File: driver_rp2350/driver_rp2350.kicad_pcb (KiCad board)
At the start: 6 copper layers, 45 x 45 mm, 0 parts

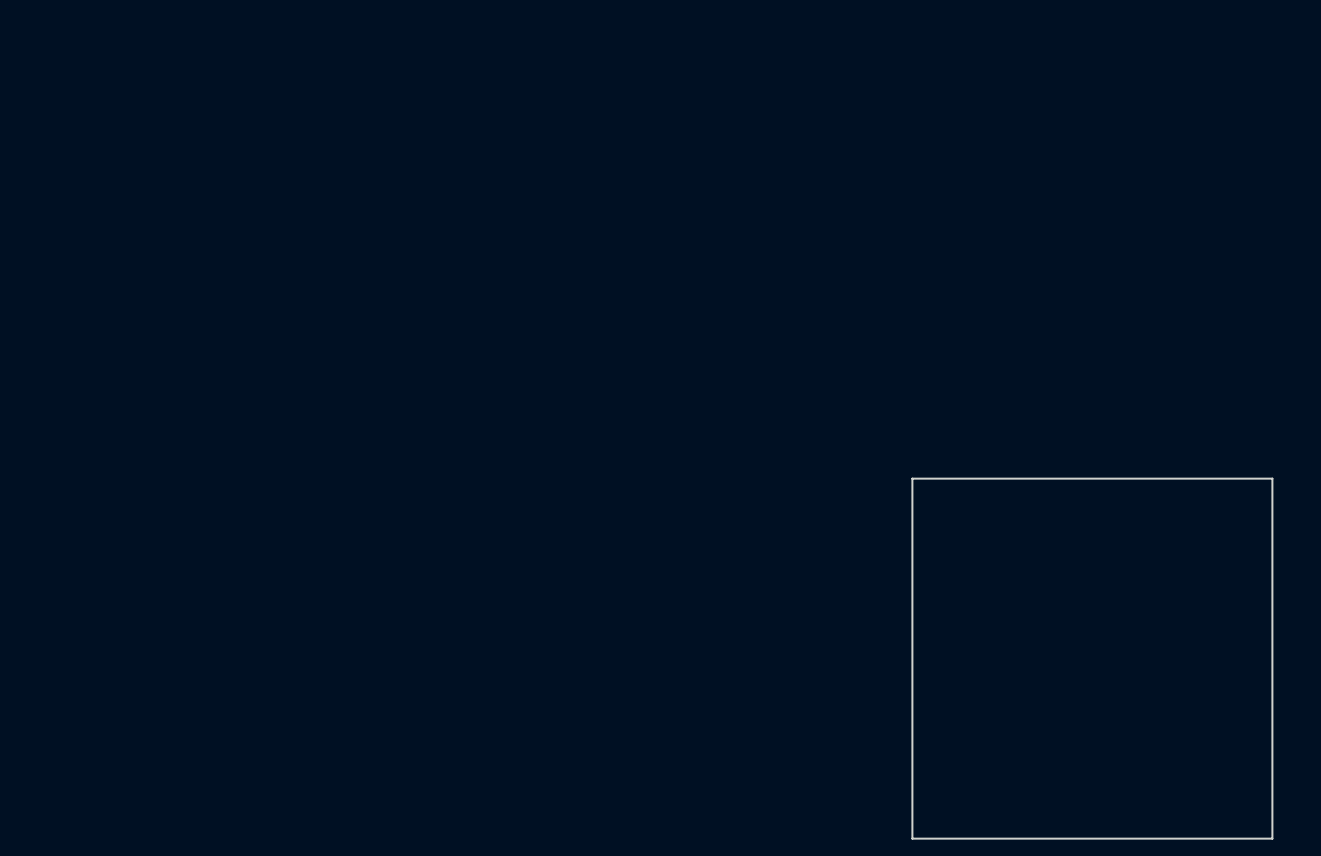
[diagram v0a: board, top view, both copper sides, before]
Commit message: Worked on rp2350 driver layout.
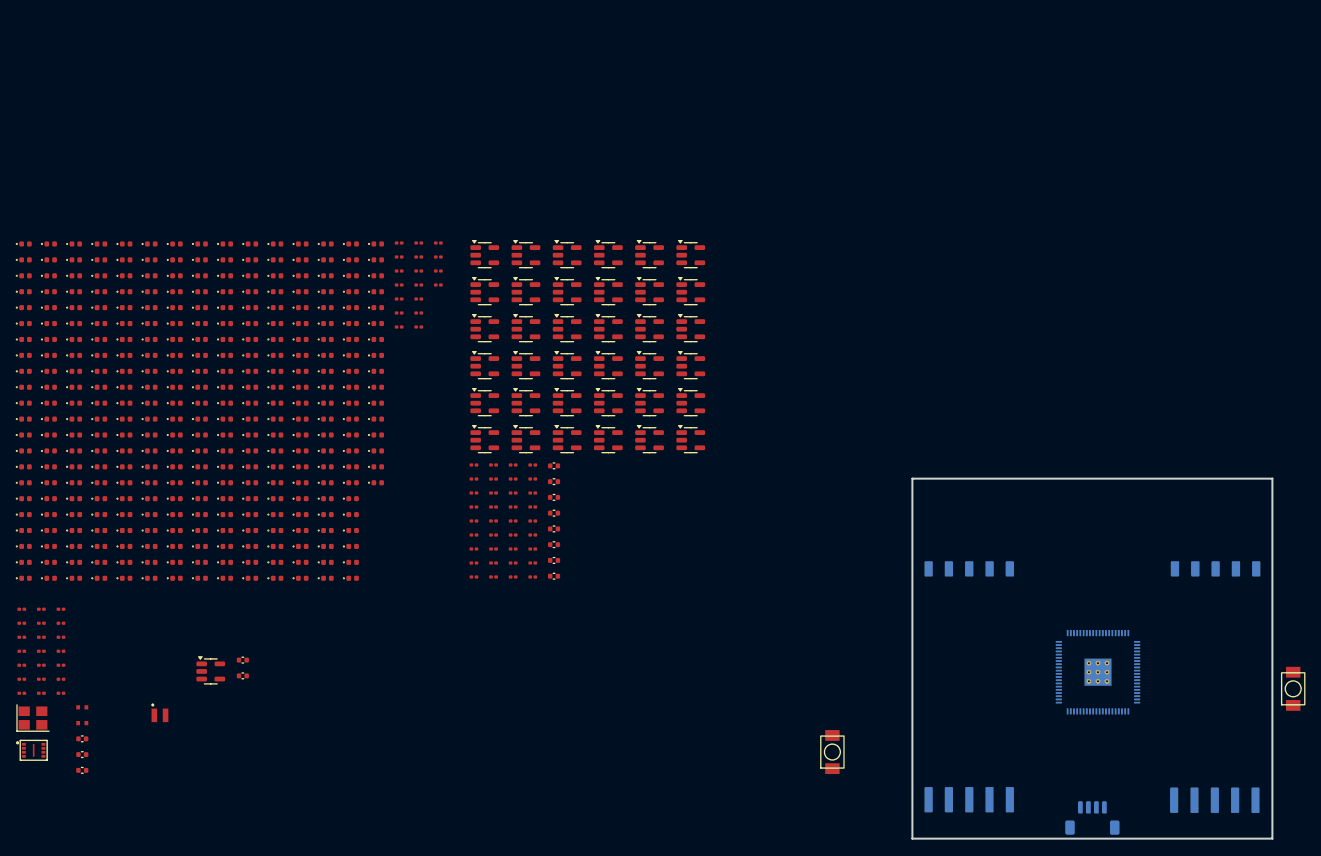
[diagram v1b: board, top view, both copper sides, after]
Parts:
- added C1: 15pF, Capacitor_SMD:C_0201_0603Metric, F.Cu at (-61.3, 66.3)
- added C10: 100nF, Capacitor_SMD:C_0201_0603Metric, F.Cu at (-61.3, 75.1)
- added C11: 100nF, Capacitor_SMD:C_0201_0603Metric, F.Cu at (-61.3, 76.8)
- added C12: 100nF, Capacitor_SMD:C_0201_0603Metric, F.Cu at (-58.9, 66.3)
- added C13: 100nF, Capacitor_SMD:C_0201_0603Metric, F.Cu at (-58.9, 68.1)
- added C14: 100nF, Capacitor_SMD:C_0201_0603Metric, F.Cu at (-58.9, 69.8)
- added C15: 100nF, Capacitor_SMD:C_0201_0603Metric, F.Cu at (-58.9, 71.6)
- added C16: 100nF, Capacitor_SMD:C_0201_0603Metric, F.Cu at (-58.9, 73.3)
- added C17: 100nF, Capacitor_SMD:C_0201_0603Metric, F.Cu at (-58.9, 75.1)
- added C18: 100nF, Capacitor_SMD:C_0201_0603Metric, F.Cu at (-58.9, 76.8)
- added C19: 10uF, Capacitor_SMD:C_0402_1005Metric, F.Cu at (-53.8, 86.5)
- added C2: 15pF, Capacitor_SMD:C_0201_0603Metric, F.Cu at (-61.3, 68.1)
- added C20: 100nF, Capacitor_SMD:C_0201_0603Metric, F.Cu at (-4.80, 48.3)
- added C21: 100nF, Capacitor_SMD:C_0201_0603Metric, F.Cu at (-4.80, 50.0)
- added C22: 100nF, Capacitor_SMD:C_0201_0603Metric, F.Cu at (-4.80, 51.8)
- added C23: 100nF, Capacitor_SMD:C_0201_0603Metric, F.Cu at (-4.80, 53.5)
- added C24: 100nF, Capacitor_SMD:C_0201_0603Metric, F.Cu at (-4.80, 55.3)
- added C25: 100nF, Capacitor_SMD:C_0201_0603Metric, F.Cu at (-4.80, 57.0)
- added C26: 100nF, Capacitor_SMD:C_0201_0603Metric, F.Cu at (-4.80, 58.8)
- added C27: 100nF, Capacitor_SMD:C_0201_0603Metric, F.Cu at (-4.80, 60.5)
- added C28: 100nF, Capacitor_SMD:C_0201_0603Metric, F.Cu at (-4.80, 62.3)
- added C29: 100nF, Capacitor_SMD:C_0201_0603Metric, F.Cu at (-2.35, 48.3)
- added C3: 100nF, Capacitor_SMD:C_0201_0603Metric, F.Cu at (-61.3, 69.8)
- added C30: 100nF, Capacitor_SMD:C_0201_0603Metric, F.Cu at (-2.35, 50.0)
- added C31: 100nF, Capacitor_SMD:C_0201_0603Metric, F.Cu at (-2.35, 51.8)
- added C32: 100nF, Capacitor_SMD:C_0201_0603Metric, F.Cu at (-2.35, 53.5)
- added C33: 100nF, Capacitor_SMD:C_0201_0603Metric, F.Cu at (-2.35, 55.3)
- added C34: 100nF, Capacitor_SMD:C_0201_0603Metric, F.Cu at (-2.35, 57.0)
- added C35: 100nF, Capacitor_SMD:C_0201_0603Metric, F.Cu at (-2.35, 58.8)
- added C36: 100nF, Capacitor_SMD:C_0201_0603Metric, F.Cu at (-2.35, 60.5)
- added C37: 100nF, Capacitor_SMD:C_0201_0603Metric, F.Cu at (-2.35, 62.3)
- added C38: 100nF, Capacitor_SMD:C_0201_0603Metric, F.Cu at (0.10, 48.3)
- added C39: 100nF, Capacitor_SMD:C_0201_0603Metric, F.Cu at (0.10, 50.0)
- added C4: 4.7uF, RP2350_80QFN_minimal:C_0402_1005Metric_small_pads, F.Cu at (-53.8, 78.6)
- added C40: 100nF, Capacitor_SMD:C_0201_0603Metric, F.Cu at (0.10, 51.8)
- added C41: 100nF, Capacitor_SMD:C_0201_0603Metric, F.Cu at (0.10, 53.5)
- added C42: 100nF, Capacitor_SMD:C_0201_0603Metric, F.Cu at (0.10, 55.3)
- added C43: 100nF, Capacitor_SMD:C_0201_0603Metric, F.Cu at (0.10, 57.0)
- added C44: 100nF, Capacitor_SMD:C_0201_0603Metric, F.Cu at (0.10, 58.8)
- added C45: 100nF, Capacitor_SMD:C_0201_0603Metric, F.Cu at (0.10, 60.5)
- added C46: 100nF, Capacitor_SMD:C_0201_0603Metric, F.Cu at (0.10, 62.3)
- added C47: 100nF, Capacitor_SMD:C_0201_0603Metric, F.Cu at (2.54, 48.3)
- added C48: 100nF, Capacitor_SMD:C_0201_0603Metric, F.Cu at (2.54, 50.0)
- added C49: 100nF, Capacitor_SMD:C_0201_0603Metric, F.Cu at (2.54, 51.8)
- added C5: 4.7uF, RP2350_80QFN_minimal:C_0402_1005Metric_small_pads, F.Cu at (-53.8, 80.6)
- added C50: 100nF, Capacitor_SMD:C_0201_0603Metric, F.Cu at (2.54, 53.5)
- added C51: 100nF, Capacitor_SMD:C_0201_0603Metric, F.Cu at (2.54, 55.3)
- added C52: 100nF, Capacitor_SMD:C_0201_0603Metric, F.Cu at (2.54, 57.0)
- added C53: 100nF, Capacitor_SMD:C_0201_0603Metric, F.Cu at (2.54, 58.8)
- added C54: 100nF, Capacitor_SMD:C_0201_0603Metric, F.Cu at (2.54, 60.5)
- added C55: 100nF, Capacitor_SMD:C_0201_0603Metric, F.Cu at (2.54, 62.3)
- added C56: 10uF, Capacitor_SMD:C_0402_1005Metric, F.Cu at (5.21, 48.4)
- added C57: 10uF, Capacitor_SMD:C_0402_1005Metric, F.Cu at (5.21, 50.4)
- added C58: 10uF, Capacitor_SMD:C_0402_1005Metric, F.Cu at (5.21, 52.3)
- added C59: 10uF, Capacitor_SMD:C_0402_1005Metric, F.Cu at (5.21, 54.3)
- added C6: 100nF, Capacitor_SMD:C_0201_0603Metric, F.Cu at (-61.3, 71.6)
- added C60: 10uF, Capacitor_SMD:C_0402_1005Metric, F.Cu at (5.21, 56.3)
- added C61: 10uF, Capacitor_SMD:C_0402_1005Metric, F.Cu at (5.21, 58.3)
- added C62: 10uF, Capacitor_SMD:C_0402_1005Metric, F.Cu at (5.21, 60.2)
- added C63: 10uF, Capacitor_SMD:C_0402_1005Metric, F.Cu at (5.21, 62.2)
- added C64: 10uF, Capacitor_SMD:C_0402_1005Metric, F.Cu at (-33.7, 72.7)
- added C65: 10uF, Capacitor_SMD:C_0402_1005Metric, F.Cu at (-33.7, 74.7)
- added C7: 4.7uF, Capacitor_SMD:C_0402_1005Metric, F.Cu at (-53.8, 82.5)
- added C8: 4.7uF, Capacitor_SMD:C_0402_1005Metric, F.Cu at (-53.8, 84.5)
- added C9: 100nF, Capacitor_SMD:C_0201_0603Metric, F.Cu at (-61.3, 73.3)
- added D_0A1: LED, panel_custom:LED_0402_1005Metric, F.Cu at (-48.3, 44.5)
- added D_0B1: LED, panel_custom:LED_0402_1005Metric, F.Cu at (-48.3, 46.5)
- added D_0C1: LED, panel_custom:LED_0402_1005Metric, F.Cu at (-48.3, 48.5)
- added D_0D1: LED, panel_custom:LED_0402_1005Metric, F.Cu at (-48.3, 50.5)
- added D_0E1: LED, panel_custom:LED_0402_1005Metric, F.Cu at (-48.3, 52.5)
- added D_0F1: LED, panel_custom:LED_0402_1005Metric, F.Cu at (-48.3, 54.5)
- added D_0G1: LED, panel_custom:LED_0402_1005Metric, F.Cu at (-48.3, 56.5)
- added D_0H1: LED, panel_custom:LED_0402_1005Metric, F.Cu at (-48.3, 58.5)
- added D_1: LED, panel_custom:LED_0402_1005Metric, F.Cu at (-60.9, 20.7)
- added D_10: LED, panel_custom:LED_0402_1005Metric, F.Cu at (-60.9, 38.6)
- added D_100: LED, panel_custom:LED_0402_1005Metric, F.Cu at (-48.3, 42.6)
- added D_11: LED, panel_custom:LED_0402_1005Metric, F.Cu at (-60.9, 40.6)
- added D_12: LED, panel_custom:LED_0402_1005Metric, F.Cu at (-60.9, 42.6)
- added D_13: LED, panel_custom:LED_0402_1005Metric, F.Cu at (-60.9, 44.5)
- added D_14: LED, panel_custom:LED_0402_1005Metric, F.Cu at (-60.9, 46.5)
- added D_15: LED, panel_custom:LED_0402_1005Metric, F.Cu at (-60.9, 48.5)
- added D_16: LED, panel_custom:LED_0402_1005Metric, F.Cu at (-60.9, 50.5)
- added D_17: LED, panel_custom:LED_0402_1005Metric, F.Cu at (-60.9, 52.5)
- added D_18: LED, panel_custom:LED_0402_1005Metric, F.Cu at (-60.9, 54.5)
- added D_19: LED, panel_custom:LED_0402_1005Metric, F.Cu at (-60.9, 56.5)
- added D_1A1: LED, panel_custom:LED_0402_1005Metric, F.Cu at (-48.3, 60.5)
- added D_1B1: LED, panel_custom:LED_0402_1005Metric, F.Cu at (-48.3, 62.5)
- added D_1C1: LED, panel_custom:LED_0402_1005Metric, F.Cu at (-45.1, 20.7)
- added D_1D1: LED, panel_custom:LED_0402_1005Metric, F.Cu at (-45.1, 22.7)
- added D_1E1: LED, panel_custom:LED_0402_1005Metric, F.Cu at (-45.1, 24.6)
- added D_1F1: LED, panel_custom:LED_0402_1005Metric, F.Cu at (-45.1, 26.6)
- added D_1G1: LED, panel_custom:LED_0402_1005Metric, F.Cu at (-45.1, 28.6)
- added D_1H1: LED, panel_custom:LED_0402_1005Metric, F.Cu at (-45.1, 30.6)
- added D_2: LED, panel_custom:LED_0402_1005Metric, F.Cu at (-60.9, 22.7)
- added D_20: LED, panel_custom:LED_0402_1005Metric, F.Cu at (-60.9, 58.5)
- added D_21: LED, panel_custom:LED_0402_1005Metric, F.Cu at (-60.9, 60.5)
- added D_22: LED, panel_custom:LED_0402_1005Metric, F.Cu at (-60.9, 62.5)
- added D_23: LED, panel_custom:LED_0402_1005Metric, F.Cu at (-57.7, 20.7)
- added D_24: LED, panel_custom:LED_0402_1005Metric, F.Cu at (-57.7, 22.7)
- added D_25: LED, panel_custom:LED_0402_1005Metric, F.Cu at (-57.7, 24.6)
- added D_26: LED, panel_custom:LED_0402_1005Metric, F.Cu at (-57.7, 26.6)
- added D_27: LED, panel_custom:LED_0402_1005Metric, F.Cu at (-57.7, 28.6)
- added D_28: LED, panel_custom:LED_0402_1005Metric, F.Cu at (-57.7, 30.6)
- added D_29: LED, panel_custom:LED_0402_1005Metric, F.Cu at (-57.7, 32.6)
- added D_2A1: LED, panel_custom:LED_0402_1005Metric, F.Cu at (-45.1, 32.6)
- added D_2B1: LED, panel_custom:LED_0402_1005Metric, F.Cu at (-45.1, 34.6)
- added D_2C1: LED, panel_custom:LED_0402_1005Metric, F.Cu at (-45.1, 36.6)
- added D_2D1: LED, panel_custom:LED_0402_1005Metric, F.Cu at (-45.1, 38.6)
- added D_2E1: LED, panel_custom:LED_0402_1005Metric, F.Cu at (-45.1, 40.6)
- added D_2F1: LED, panel_custom:LED_0402_1005Metric, F.Cu at (-45.1, 42.6)
- added D_2G1: LED, panel_custom:LED_0402_1005Metric, F.Cu at (-45.1, 44.5)
- added D_2H1: LED, panel_custom:LED_0402_1005Metric, F.Cu at (-45.1, 46.5)
- added D_3: LED, panel_custom:LED_0402_1005Metric, F.Cu at (-60.9, 24.6)
- added D_30: LED, panel_custom:LED_0402_1005Metric, F.Cu at (-57.7, 34.6)
- added D_31: LED, panel_custom:LED_0402_1005Metric, F.Cu at (-57.7, 36.6)
- added D_32: LED, panel_custom:LED_0402_1005Metric, F.Cu at (-57.7, 38.6)
- added D_33: LED, panel_custom:LED_0402_1005Metric, F.Cu at (-57.7, 40.6)
- added D_34: LED, panel_custom:LED_0402_1005Metric, F.Cu at (-57.7, 42.6)
- added D_35: LED, panel_custom:LED_0402_1005Metric, F.Cu at (-57.7, 44.5)
- added D_36: LED, panel_custom:LED_0402_1005Metric, F.Cu at (-57.7, 46.5)
- added D_37: LED, panel_custom:LED_0402_1005Metric, F.Cu at (-57.7, 48.5)
- added D_38: LED, panel_custom:LED_0402_1005Metric, F.Cu at (-57.7, 50.5)
- added D_39: LED, panel_custom:LED_0402_1005Metric, F.Cu at (-57.7, 52.5)
- added D_3A1: LED, panel_custom:LED_0402_1005Metric, F.Cu at (-45.1, 48.5)
- added D_3B1: LED, panel_custom:LED_0402_1005Metric, F.Cu at (-45.1, 50.5)
- added D_3C1: LED, panel_custom:LED_0402_1005Metric, F.Cu at (-45.1, 52.5)
- added D_3D1: LED, panel_custom:LED_0402_1005Metric, F.Cu at (-45.1, 54.5)
- added D_3E1: LED, panel_custom:LED_0402_1005Metric, F.Cu at (-45.1, 56.5)
- added D_3F1: LED, panel_custom:LED_0402_1005Metric, F.Cu at (-45.1, 58.5)
- added D_3G1: LED, panel_custom:LED_0402_1005Metric, F.Cu at (-45.1, 60.5)
- added D_3H1: LED, panel_custom:LED_0402_1005Metric, F.Cu at (-45.1, 62.5)
- added D_4: LED, panel_custom:LED_0402_1005Metric, F.Cu at (-60.9, 26.6)
- added D_40: LED, panel_custom:LED_0402_1005Metric, F.Cu at (-57.7, 54.5)
- added D_41: LED, panel_custom:LED_0402_1005Metric, F.Cu at (-57.7, 56.5)
- added D_42: LED, panel_custom:LED_0402_1005Metric, F.Cu at (-57.7, 58.5)
- added D_43: LED, panel_custom:LED_0402_1005Metric, F.Cu at (-57.7, 60.5)
- added D_44: LED, panel_custom:LED_0402_1005Metric, F.Cu at (-57.7, 62.5)
- added D_45: LED, panel_custom:LED_0402_1005Metric, F.Cu at (-54.6, 20.7)
- added D_46: LED, panel_custom:LED_0402_1005Metric, F.Cu at (-54.6, 22.7)
- added D_47: LED, panel_custom:LED_0402_1005Metric, F.Cu at (-54.6, 24.6)
- added D_48: LED, panel_custom:LED_0402_1005Metric, F.Cu at (-54.6, 26.6)
- added D_49: LED, panel_custom:LED_0402_1005Metric, F.Cu at (-54.6, 28.6)
- added D_4A1: LED, panel_custom:LED_0402_1005Metric, F.Cu at (-42.0, 20.7)
- added D_4B1: LED, panel_custom:LED_0402_1005Metric, F.Cu at (-42.0, 22.7)
- added D_4C1: LED, panel_custom:LED_0402_1005Metric, F.Cu at (-42.0, 24.6)
- added D_4D1: LED, panel_custom:LED_0402_1005Metric, F.Cu at (-42.0, 26.6)
- added D_4E1: LED, panel_custom:LED_0402_1005Metric, F.Cu at (-42.0, 28.6)
- added D_4F1: LED, panel_custom:LED_0402_1005Metric, F.Cu at (-42.0, 30.6)
- added D_4G1: LED, panel_custom:LED_0402_1005Metric, F.Cu at (-42.0, 32.6)
- added D_4H1: LED, panel_custom:LED_0402_1005Metric, F.Cu at (-42.0, 34.6)
- added D_5: LED, panel_custom:LED_0402_1005Metric, F.Cu at (-60.9, 28.6)
- added D_50: LED, panel_custom:LED_0402_1005Metric, F.Cu at (-54.6, 30.6)
- added D_51: LED, panel_custom:LED_0402_1005Metric, F.Cu at (-54.6, 32.6)
- added D_52: LED, panel_custom:LED_0402_1005Metric, F.Cu at (-54.6, 34.6)
- added D_53: LED, panel_custom:LED_0402_1005Metric, F.Cu at (-54.6, 36.6)
- added D_54: LED, panel_custom:LED_0402_1005Metric, F.Cu at (-54.6, 38.6)
- added D_55: LED, panel_custom:LED_0402_1005Metric, F.Cu at (-54.6, 40.6)
- added D_56: LED, panel_custom:LED_0402_1005Metric, F.Cu at (-54.6, 42.6)
- added D_57: LED, panel_custom:LED_0402_1005Metric, F.Cu at (-54.6, 44.5)
- added D_58: LED, panel_custom:LED_0402_1005Metric, F.Cu at (-54.6, 46.5)
- added D_59: LED, panel_custom:LED_0402_1005Metric, F.Cu at (-54.6, 48.5)
- added D_5A1: LED, panel_custom:LED_0402_1005Metric, F.Cu at (-42.0, 36.6)
- added D_5B1: LED, panel_custom:LED_0402_1005Metric, F.Cu at (-42.0, 38.6)
- added D_5C1: LED, panel_custom:LED_0402_1005Metric, F.Cu at (-42.0, 40.6)
- added D_5D1: LED, panel_custom:LED_0402_1005Metric, F.Cu at (-42.0, 42.6)
- added D_5E1: LED, panel_custom:LED_0402_1005Metric, F.Cu at (-42.0, 44.5)
- added D_5F1: LED, panel_custom:LED_0402_1005Metric, F.Cu at (-42.0, 46.5)
- added D_5G1: LED, panel_custom:LED_0402_1005Metric, F.Cu at (-42.0, 48.5)
- added D_5H1: LED, panel_custom:LED_0402_1005Metric, F.Cu at (-42.0, 50.5)
- added D_6: LED, panel_custom:LED_0402_1005Metric, F.Cu at (-60.9, 30.6)
- added D_60: LED, panel_custom:LED_0402_1005Metric, F.Cu at (-54.6, 50.5)
- added D_61: LED, panel_custom:LED_0402_1005Metric, F.Cu at (-54.6, 52.5)
- added D_62: LED, panel_custom:LED_0402_1005Metric, F.Cu at (-54.6, 54.5)
- added D_63: LED, panel_custom:LED_0402_1005Metric, F.Cu at (-54.6, 56.5)
- added D_64: LED, panel_custom:LED_0402_1005Metric, F.Cu at (-54.6, 58.5)
- added D_65: LED, panel_custom:LED_0402_1005Metric, F.Cu at (-54.6, 60.5)
- added D_66: LED, panel_custom:LED_0402_1005Metric, F.Cu at (-54.6, 62.5)
- added D_67: LED, panel_custom:LED_0402_1005Metric, F.Cu at (-51.4, 20.7)
- added D_68: LED, panel_custom:LED_0402_1005Metric, F.Cu at (-51.4, 22.7)
- added D_69: LED, panel_custom:LED_0402_1005Metric, F.Cu at (-51.4, 24.6)
- added D_6A1: LED, panel_custom:LED_0402_1005Metric, F.Cu at (-42.0, 52.5)
- added D_6B1: LED, panel_custom:LED_0402_1005Metric, F.Cu at (-42.0, 54.5)
- added D_6C1: LED, panel_custom:LED_0402_1005Metric, F.Cu at (-42.0, 56.5)
- added D_6D1: LED, panel_custom:LED_0402_1005Metric, F.Cu at (-42.0, 58.5)
- added D_6E1: LED, panel_custom:LED_0402_1005Metric, F.Cu at (-42.0, 60.5)
- added D_6F1: LED, panel_custom:LED_0402_1005Metric, F.Cu at (-42.0, 62.5)
- added D_6G1: LED, panel_custom:LED_0402_1005Metric, F.Cu at (-38.8, 20.7)
- added D_6H1: LED, panel_custom:LED_0402_1005Metric, F.Cu at (-38.8, 22.7)
- added D_7: LED, panel_custom:LED_0402_1005Metric, F.Cu at (-60.9, 32.6)
- added D_70: LED, panel_custom:LED_0402_1005Metric, F.Cu at (-51.4, 26.6)
- added D_71: LED, panel_custom:LED_0402_1005Metric, F.Cu at (-51.4, 28.6)
- added D_72: LED, panel_custom:LED_0402_1005Metric, F.Cu at (-51.4, 30.6)
- added D_73: LED, panel_custom:LED_0402_1005Metric, F.Cu at (-51.4, 32.6)
- added D_74: LED, panel_custom:LED_0402_1005Metric, F.Cu at (-51.4, 34.6)
- added D_75: LED, panel_custom:LED_0402_1005Metric, F.Cu at (-51.4, 36.6)
- added D_76: LED, panel_custom:LED_0402_1005Metric, F.Cu at (-51.4, 38.6)
- added D_77: LED, panel_custom:LED_0402_1005Metric, F.Cu at (-51.4, 40.6)
- added D_78: LED, panel_custom:LED_0402_1005Metric, F.Cu at (-51.4, 42.6)
- added D_79: LED, panel_custom:LED_0402_1005Metric, F.Cu at (-51.4, 44.5)
- added D_7A1: LED, panel_custom:LED_0402_1005Metric, F.Cu at (-38.8, 24.6)
- added D_7B1: LED, panel_custom:LED_0402_1005Metric, F.Cu at (-38.8, 26.6)
- added D_7C1: LED, panel_custom:LED_0402_1005Metric, F.Cu at (-38.8, 28.6)
- added D_7D1: LED, panel_custom:LED_0402_1005Metric, F.Cu at (-38.8, 30.6)
- added D_7E1: LED, panel_custom:LED_0402_1005Metric, F.Cu at (-38.8, 32.6)
- added D_7F1: LED, panel_custom:LED_0402_1005Metric, F.Cu at (-38.8, 34.6)
- added D_7G1: LED, panel_custom:LED_0402_1005Metric, F.Cu at (-38.8, 36.6)
- added D_7H1: LED, panel_custom:LED_0402_1005Metric, F.Cu at (-38.8, 38.6)
- added D_8: LED, panel_custom:LED_0402_1005Metric, F.Cu at (-60.9, 34.6)
- added D_80: LED, panel_custom:LED_0402_1005Metric, F.Cu at (-51.4, 46.5)
- added D_81: LED, panel_custom:LED_0402_1005Metric, F.Cu at (-51.4, 48.5)
- added D_82: LED, panel_custom:LED_0402_1005Metric, F.Cu at (-51.4, 50.5)
- added D_83: LED, panel_custom:LED_0402_1005Metric, F.Cu at (-51.4, 52.5)
- added D_84: LED, panel_custom:LED_0402_1005Metric, F.Cu at (-51.4, 54.5)
- added D_85: LED, panel_custom:LED_0402_1005Metric, F.Cu at (-51.4, 56.5)
- added D_86: LED, panel_custom:LED_0402_1005Metric, F.Cu at (-51.4, 58.5)
- added D_87: LED, panel_custom:LED_0402_1005Metric, F.Cu at (-51.4, 60.5)
- added D_88: LED, panel_custom:LED_0402_1005Metric, F.Cu at (-51.4, 62.5)
- added D_89: LED, panel_custom:LED_0402_1005Metric, F.Cu at (-48.3, 20.7)
- added D_8A1: LED, panel_custom:LED_0402_1005Metric, F.Cu at (-38.8, 40.6)
- added D_8B1: LED, panel_custom:LED_0402_1005Metric, F.Cu at (-38.8, 42.6)
- added D_8C1: LED, panel_custom:LED_0402_1005Metric, F.Cu at (-38.8, 44.5)
- added D_8D1: LED, panel_custom:LED_0402_1005Metric, F.Cu at (-38.8, 46.5)
- added D_8E1: LED, panel_custom:LED_0402_1005Metric, F.Cu at (-38.8, 48.5)
- added D_8F1: LED, panel_custom:LED_0402_1005Metric, F.Cu at (-38.8, 50.5)
- added D_8G1: LED, panel_custom:LED_0402_1005Metric, F.Cu at (-38.8, 52.5)
- added D_8H1: LED, panel_custom:LED_0402_1005Metric, F.Cu at (-38.8, 54.5)
- added D_9: LED, panel_custom:LED_0402_1005Metric, F.Cu at (-60.9, 36.6)
- added D_90: LED, panel_custom:LED_0402_1005Metric, F.Cu at (-48.3, 22.7)
- added D_91: LED, panel_custom:LED_0402_1005Metric, F.Cu at (-48.3, 24.6)
- added D_92: LED, panel_custom:LED_0402_1005Metric, F.Cu at (-48.3, 26.6)
- added D_93: LED, panel_custom:LED_0402_1005Metric, F.Cu at (-48.3, 28.6)
- added D_94: LED, panel_custom:LED_0402_1005Metric, F.Cu at (-48.3, 30.6)
- added D_95: LED, panel_custom:LED_0402_1005Metric, F.Cu at (-48.3, 32.6)
- added D_96: LED, panel_custom:LED_0402_1005Metric, F.Cu at (-48.3, 34.6)
- added D_97: LED, panel_custom:LED_0402_1005Metric, F.Cu at (-48.3, 36.6)
- added D_98: LED, panel_custom:LED_0402_1005Metric, F.Cu at (-48.3, 38.6)
- added D_99: LED, panel_custom:LED_0402_1005Metric, F.Cu at (-48.3, 40.6)
- added D_9A1: LED, panel_custom:LED_0402_1005Metric, F.Cu at (-38.8, 56.5)
- added D_9B1: LED, panel_custom:LED_0402_1005Metric, F.Cu at (-38.8, 58.5)
- added D_9C1: LED, panel_custom:LED_0402_1005Metric, F.Cu at (-38.8, 60.5)
- added D_9D1: LED, panel_custom:LED_0402_1005Metric, F.Cu at (-38.8, 62.5)
- added D_9E1: LED, panel_custom:LED_0402_1005Metric, F.Cu at (-35.7, 20.7)
- added D_9F1: LED, panel_custom:LED_0402_1005Metric, F.Cu at (-35.7, 22.7)
- added D_9G1: LED, panel_custom:LED_0402_1005Metric, F.Cu at (-35.7, 24.6)
- added D_9H1: LED, panel_custom:LED_0402_1005Metric, F.Cu at (-35.7, 26.6)
- added D_A1: LED, panel_custom:LED_0402_1005Metric, F.Cu at (-35.7, 28.6)
- added D_A10: LED, panel_custom:LED_0402_1005Metric, F.Cu at (-35.7, 46.5)
- added D_A2: LED, panel_custom:LED_0402_1005Metric, F.Cu at (-35.7, 30.6)
- added D_A3: LED, panel_custom:LED_0402_1005Metric, F.Cu at (-35.7, 32.6)
- added D_A4: LED, panel_custom:LED_0402_1005Metric, F.Cu at (-35.7, 34.6)
- added D_A5: LED, panel_custom:LED_0402_1005Metric, F.Cu at (-35.7, 36.6)
- added D_A6: LED, panel_custom:LED_0402_1005Metric, F.Cu at (-35.7, 38.6)
- added D_A7: LED, panel_custom:LED_0402_1005Metric, F.Cu at (-35.7, 40.6)
- added D_A8: LED, panel_custom:LED_0402_1005Metric, F.Cu at (-35.7, 42.6)
- added D_A9: LED, panel_custom:LED_0402_1005Metric, F.Cu at (-35.7, 44.5)
- added D_AA1: LED, panel_custom:LED_0402_1005Metric, F.Cu at (-35.7, 48.5)
- added D_AB1: LED, panel_custom:LED_0402_1005Metric, F.Cu at (-35.7, 50.5)
- added D_AC1: LED, panel_custom:LED_0402_1005Metric, F.Cu at (-35.7, 52.5)
- added D_AD1: LED, panel_custom:LED_0402_1005Metric, F.Cu at (-35.7, 54.5)
- added D_AE1: LED, panel_custom:LED_0402_1005Metric, F.Cu at (-35.7, 56.5)
- added D_AF1: LED, panel_custom:LED_0402_1005Metric, F.Cu at (-35.7, 58.5)
- added D_AG1: LED, panel_custom:LED_0402_1005Metric, F.Cu at (-35.7, 60.5)
- added D_AH1: LED, panel_custom:LED_0402_1005Metric, F.Cu at (-35.7, 62.5)
- added D_B1: LED, panel_custom:LED_0402_1005Metric, F.Cu at (-32.6, 20.7)
- added D_B10: LED, panel_custom:LED_0402_1005Metric, F.Cu at (-32.6, 38.6)
- added D_B2: LED, panel_custom:LED_0402_1005Metric, F.Cu at (-32.6, 22.7)
- added D_B3: LED, panel_custom:LED_0402_1005Metric, F.Cu at (-32.6, 24.6)
- added D_B4: LED, panel_custom:LED_0402_1005Metric, F.Cu at (-32.6, 26.6)
- added D_B5: LED, panel_custom:LED_0402_1005Metric, F.Cu at (-32.6, 28.6)
- added D_B6: LED, panel_custom:LED_0402_1005Metric, F.Cu at (-32.6, 30.6)
- added D_B7: LED, panel_custom:LED_0402_1005Metric, F.Cu at (-32.6, 32.6)
- added D_B8: LED, panel_custom:LED_0402_1005Metric, F.Cu at (-32.6, 34.6)
- added D_B9: LED, panel_custom:LED_0402_1005Metric, F.Cu at (-32.6, 36.6)
- added D_BA1: LED, panel_custom:LED_0402_1005Metric, F.Cu at (-32.6, 40.6)
- added D_BB1: LED, panel_custom:LED_0402_1005Metric, F.Cu at (-32.6, 42.6)
- added D_BC1: LED, panel_custom:LED_0402_1005Metric, F.Cu at (-32.6, 44.5)
- added D_BD1: LED, panel_custom:LED_0402_1005Metric, F.Cu at (-32.6, 46.5)
- added D_BE1: LED, panel_custom:LED_0402_1005Metric, F.Cu at (-32.6, 48.5)
- added D_BF1: LED, panel_custom:LED_0402_1005Metric, F.Cu at (-32.6, 50.5)
- added D_BG1: LED, panel_custom:LED_0402_1005Metric, F.Cu at (-32.6, 52.5)
- added D_BH1: LED, panel_custom:LED_0402_1005Metric, F.Cu at (-32.6, 54.5)
- added D_C1: LED, panel_custom:LED_0402_1005Metric, F.Cu at (-32.6, 56.5)
- added D_C10: LED, panel_custom:LED_0402_1005Metric, F.Cu at (-29.4, 30.6)
- added D_C2: LED, panel_custom:LED_0402_1005Metric, F.Cu at (-32.6, 58.5)
- added D_C3: LED, panel_custom:LED_0402_1005Metric, F.Cu at (-32.6, 60.5)
- added D_C4: LED, panel_custom:LED_0402_1005Metric, F.Cu at (-32.6, 62.5)
- added D_C5: LED, panel_custom:LED_0402_1005Metric, F.Cu at (-29.4, 20.7)
- added D_C6: LED, panel_custom:LED_0402_1005Metric, F.Cu at (-29.4, 22.7)
- added D_C7: LED, panel_custom:LED_0402_1005Metric, F.Cu at (-29.4, 24.6)
- added D_C8: LED, panel_custom:LED_0402_1005Metric, F.Cu at (-29.4, 26.6)
- added D_C9: LED, panel_custom:LED_0402_1005Metric, F.Cu at (-29.4, 28.6)
- added D_CA1: LED, panel_custom:LED_0402_1005Metric, F.Cu at (-29.4, 32.6)
- added D_CB1: LED, panel_custom:LED_0402_1005Metric, F.Cu at (-29.4, 34.6)
- added D_CC1: LED, panel_custom:LED_0402_1005Metric, F.Cu at (-29.4, 36.6)
- added D_CD1: LED, panel_custom:LED_0402_1005Metric, F.Cu at (-29.4, 38.6)
- added D_CE1: LED, panel_custom:LED_0402_1005Metric, F.Cu at (-29.4, 40.6)
- added D_CF1: LED, panel_custom:LED_0402_1005Metric, F.Cu at (-29.4, 42.6)
- added D_CG1: LED, panel_custom:LED_0402_1005Metric, F.Cu at (-29.4, 44.5)
- added D_CH1: LED, panel_custom:LED_0402_1005Metric, F.Cu at (-29.4, 46.5)
- added D_D1: LED, panel_custom:LED_0402_1005Metric, F.Cu at (-29.4, 48.5)
- added D_D10: LED, panel_custom:LED_0402_1005Metric, F.Cu at (-26.3, 22.7)
- added D_D2: LED, panel_custom:LED_0402_1005Metric, F.Cu at (-29.4, 50.5)
- added D_D3: LED, panel_custom:LED_0402_1005Metric, F.Cu at (-29.4, 52.5)
- added D_D4: LED, panel_custom:LED_0402_1005Metric, F.Cu at (-29.4, 54.5)
- added D_D5: LED, panel_custom:LED_0402_1005Metric, F.Cu at (-29.4, 56.5)
- added D_D6: LED, panel_custom:LED_0402_1005Metric, F.Cu at (-29.4, 58.5)
- added D_D7: LED, panel_custom:LED_0402_1005Metric, F.Cu at (-29.4, 60.5)
- added D_D8: LED, panel_custom:LED_0402_1005Metric, F.Cu at (-29.4, 62.5)
- added D_D9: LED, panel_custom:LED_0402_1005Metric, F.Cu at (-26.3, 20.7)
- added D_DA1: LED, panel_custom:LED_0402_1005Metric, F.Cu at (-26.3, 24.6)
- added D_DB1: LED, panel_custom:LED_0402_1005Metric, F.Cu at (-26.3, 26.6)
- added D_DC1: LED, panel_custom:LED_0402_1005Metric, F.Cu at (-26.3, 28.6)
- added D_DD1: LED, panel_custom:LED_0402_1005Metric, F.Cu at (-26.3, 30.6)
- added D_DE1: LED, panel_custom:LED_0402_1005Metric, F.Cu at (-26.3, 32.6)
- added D_DF1: LED, panel_custom:LED_0402_1005Metric, F.Cu at (-26.3, 34.6)
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
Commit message: Modified for rp2354.
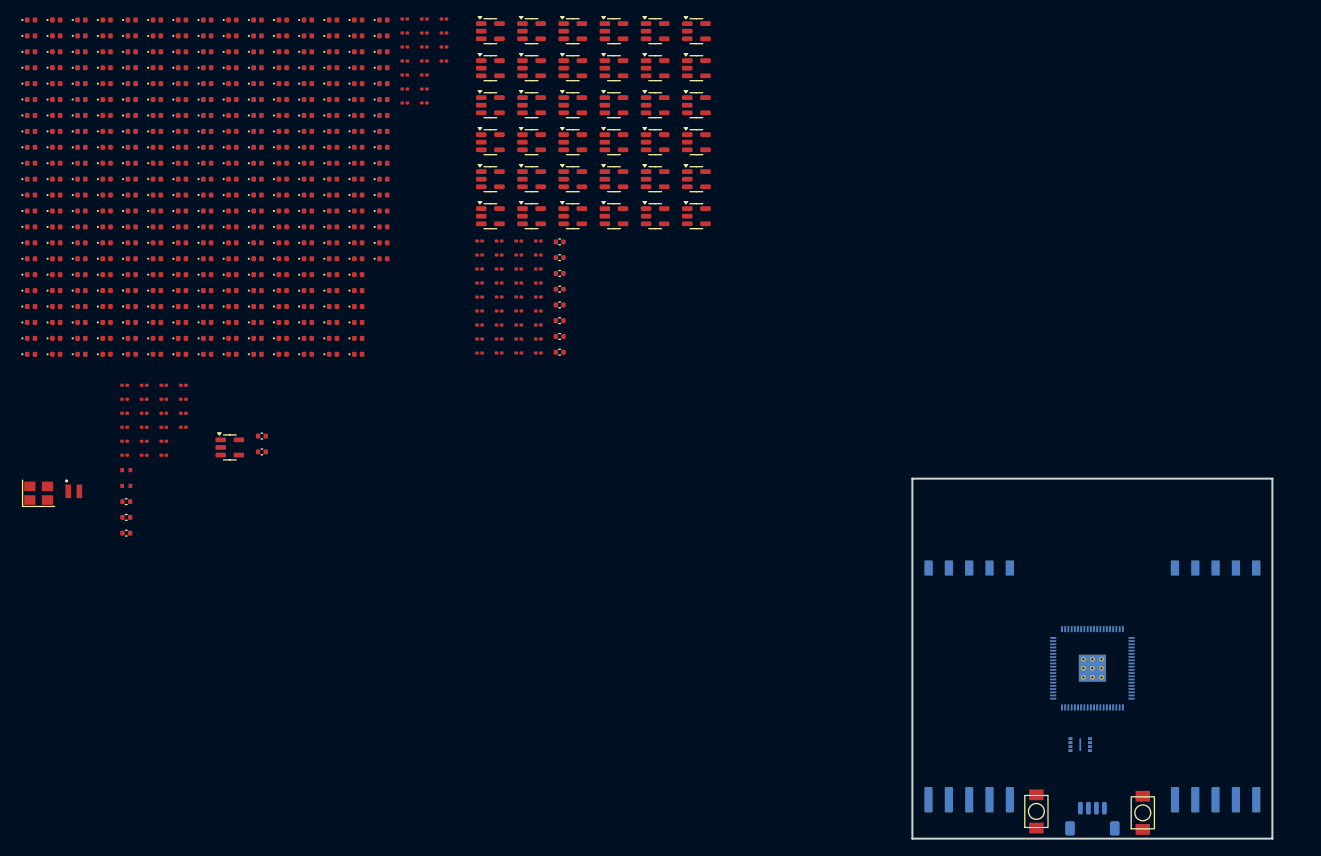
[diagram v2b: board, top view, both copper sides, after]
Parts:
- added R26: 270, Resistor_SMD:R_0201_0603Metric, F.Cu at (-8.55, -2.21)
- R4: value 33 -> 10k
- R6: value 27 -> 33
- R8: value 270 -> 27
- U1: value W25Q16JVUXIQ_TR -> APS6404L-3SQR; moved to B.Cu
- U2: value RP2350_80QFN -> RP2354B_80QFN
- moved U1 130.8 mm to (71.0, 83.2)
- moved C11 41.4 mm to (-46.0, 38.3)
- moved C17 39.8 mm to (-43.6, 38.3)
- moved C18 39.8 mm to (-43.6, 40.1)
- moved SW2 39.5 mm to (78.8, 91.8)
- moved R5 38.2 mm to (-41.1, 38.3)
- moved R6 38.2 mm to (-41.1, 40.1)
- moved R7 38.2 mm to (-41.1, 41.8)
- moved SW1 35.6 mm to (65.5, 91.6)
- moved R8 35.5 mm to (-41.1, 43.6)
- moved C1 30.8 mm to (-48.5, 38.3)
- moved C10 30.8 mm to (-48.5, 47.1)
- moved C2 30.8 mm to (-48.5, 40.1)
- moved C3 30.8 mm to (-48.5, 41.8)
- moved C6 30.8 mm to (-48.5, 43.6)
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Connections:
- C65 pad 1: +3.3V -> +3V3
- R1 pad 2: /panel_mcu/QSPI_SS -> /panel_mcu/XIP_CS1n
- R10 pad 1: /drivers/COL_2 -> /drivers/COL_1
- R10 pad 2: Net-(D_21-A) -> Net-(D_11-A)
- R11 pad 1: /drivers/COL_3 -> /drivers/COL_2
- R11 pad 2: Net-(D_31-A) -> Net-(D_21-A)
- R12 pad 1: /drivers/COL_4 -> /drivers/COL_3
- R12 pad 2: Net-(D_41-A) -> Net-(D_31-A)
- R13 pad 1: /drivers/COL_5 -> /drivers/COL_4
- R13 pad 2: Net-(D_51-A) -> Net-(D_41-A)
- R14 pad 1: /drivers/COL_6 -> /drivers/COL_5
- R14 pad 2: Net-(D_61-A) -> Net-(D_51-A)
- R15 pad 1: /drivers/COL_7 -> /drivers/COL_6
- R15 pad 2: Net-(D_71-A) -> Net-(D_61-A)
- R16 pad 1: /drivers/COL_8 -> /drivers/COL_7
- R16 pad 2: Net-(D_81-A) -> Net-(D_71-A)
- R17 pad 1: /drivers/COL_9 -> /drivers/COL_8
- R17 pad 2: Net-(D_100-A) -> Net-(D_81-A)
- R18 pad 1: /drivers/COL_A -> /drivers/COL_9
- R18 pad 2: Net-(D_0A1-A) -> Net-(D_100-A)
- R19 pad 1: /drivers/COL_B -> /drivers/COL_A
- R19 pad 2: Net-(D_0B1-A) -> Net-(D_0A1-A)
- R2 pad 1: /panel_mcu/XOUT -> Net-(R2-Pad1)
- R2 pad 2: Net-(C2-Pad1) -> GND
- R20 pad 1: /drivers/COL_C -> /drivers/COL_B
- R20 pad 2: Net-(D_0C1-A) -> Net-(D_0B1-A)
- R21 pad 1: /drivers/COL_D -> /drivers/COL_C
- R21 pad 2: Net-(D_0D1-A) -> Net-(D_0C1-A)
- R22 pad 1: /drivers/COL_E -> /drivers/COL_D
- R22 pad 2: Net-(D_0E1-A) -> Net-(D_0D1-A)
- R23 pad 1: /drivers/COL_F -> /drivers/COL_E
- R23 pad 2: Net-(D_0F1-A) -> Net-(D_0E1-A)
- R24 pad 1: /drivers/COL_G -> /drivers/COL_F
- R24 pad 2: Net-(D_0G1-A) -> Net-(D_0F1-A)
- R25 pad 1: /drivers/COL_H -> /drivers/COL_G
- R25 pad 2: Net-(D_0H1-A) -> Net-(D_0G1-A)
- R3 pad 1: Net-(R3-Pad1) -> /panel_mcu/QSPI_SS
- R3 pad 2: GND -> /panel_mcu/~{USB_BOOT}
- R4 pad 2: /panel_mcu/VREG_AVDD -> /panel_mcu/QSPI_SS
- R5 pad 1: /panel_mcu/QSPI_SS -> /panel_mcu/XOUT
- R5 pad 2: /panel_mcu/~{USB_BOOT} -> Net-(C2-Pad1)
- R6 pad 1: /panel_mcu/D+ -> +3V3
- R6 pad 2: Net-(U2-USB_DP) -> /panel_mcu/VREG_AVDD
- R7 pad 1: /panel_mcu/D- -> /panel_mcu/D+
- R7 pad 2: Net-(U2-USB_DM) -> Net-(U2-USB_DP)
- R8 pad 1: /drivers/COL_0 -> /panel_mcu/D-
- R8 pad 2: Net-(D_1-A) -> Net-(U2-USB_DM)
- R9 pad 1: /drivers/COL_1 -> /drivers/COL_0
- R9 pad 2: Net-(D_11-A) -> Net-(D_1-A)
- SW2 pad 1: Net-(R3-Pad1) -> Net-(R2-Pad1)
- U1 pad 1: /panel_mcu/QSPI_SS -> /panel_mcu/XIP_CS1n
- U2 pad 1: /drivers/COL_MCU_4 -> /drivers/COL_MCU_3
- U2 pad 11: /drivers/COL_MCU_C -> /drivers/COL_MCU_B
- U2 pad 12: /drivers/COL_MCU_D -> /drivers/COL_MCU_C
- U2 pad 13: /drivers/COL_MCU_E -> /drivers/COL_MCU_D
- U2 pad 14: /drivers/COL_MCU_F -> /drivers/COL_MCU_E
- U2 pad 16: /drivers/COL_MCU_G -> /drivers/COL_MCU_F
- U2 pad 17: /drivers/COL_MCU_H -> /drivers/COL_MCU_G
- U2 pad 18: /drivers/ROW_MCU_0 -> /drivers/COL_MCU_H
- U2 pad 19: /drivers/ROW_MCU_1 -> /drivers/ROW_MCU_0
- U2 pad 2: /drivers/COL_MCU_5 -> /drivers/COL_MCU_4
- U2 pad 20: /drivers/ROW_MCU_2 -> /drivers/ROW_MCU_1
- U2 pad 21: /drivers/ROW_MCU_3 -> /drivers/ROW_MCU_2
- U2 pad 22: /drivers/ROW_MCU_4 -> /drivers/ROW_MCU_3
- U2 pad 23: /drivers/ROW_MCU_5 -> /drivers/ROW_MCU_4
- U2 pad 25: /drivers/ROW_MCU_6 -> /drivers/ROW_MCU_5
- U2 pad 26: /drivers/ROW_MCU_7 -> /drivers/ROW_MCU_6
- U2 pad 27: /drivers/ROW_MCU_8 -> /drivers/ROW_MCU_7
- U2 pad 28: /drivers/ROW_MCU_9 -> /drivers/ROW_MCU_8
- U2 pad 3: /drivers/COL_MCU_6 -> /drivers/COL_MCU_5
- U2 pad 36: /drivers/ROW_MCU_A -> /drivers/ROW_MCU_9
- U2 pad 37: /drivers/ROW_MCU_B -> /drivers/ROW_MCU_A
- U2 pad 38: /drivers/ROW_MCU_C -> /drivers/ROW_MCU_B
- U2 pad 39: /drivers/ROW_MCU_D -> /drivers/ROW_MCU_C
- U2 pad 4: /drivers/COL_MCU_7 -> /drivers/COL_MCU_6
- U2 pad 45: /drivers/ROW_MCU_E -> /drivers/ROW_MCU_D
- U2 pad 46: /drivers/ROW_MCU_F -> /drivers/ROW_MCU_E
- U2 pad 47: /drivers/ROW_MCU_H -> /drivers/ROW_MCU_F
- U2 pad 48: /drivers/ROW_MCU_G -> /drivers/ROW_MCU_H
- U2 pad 49: unconnected-(U2-GPIO40_ADC0-Pad49) -> /drivers/ROW_MCU_G
- U2 pad 6: /drivers/COL_MCU_8 -> /drivers/COL_MCU_7
- U2 pad 7: /drivers/COL_MCU_9 -> /drivers/COL_MCU_8
- U2 pad 77: /drivers/COL_MCU_0 -> /panel_mcu/XIP_CS1n
- U2 pad 78: /drivers/COL_MCU_1 -> /drivers/COL_MCU_0
- U2 pad 79: /drivers/COL_MCU_2 -> /drivers/COL_MCU_1
- U2 pad 8: /drivers/COL_MCU_A -> /drivers/COL_MCU_9
- U2 pad 80: /drivers/COL_MCU_3 -> /drivers/COL_MCU_2
- U2 pad 9: /drivers/COL_MCU_B -> /drivers/COL_MCU_A
- U39 pad 5: +3.3V -> +3V3

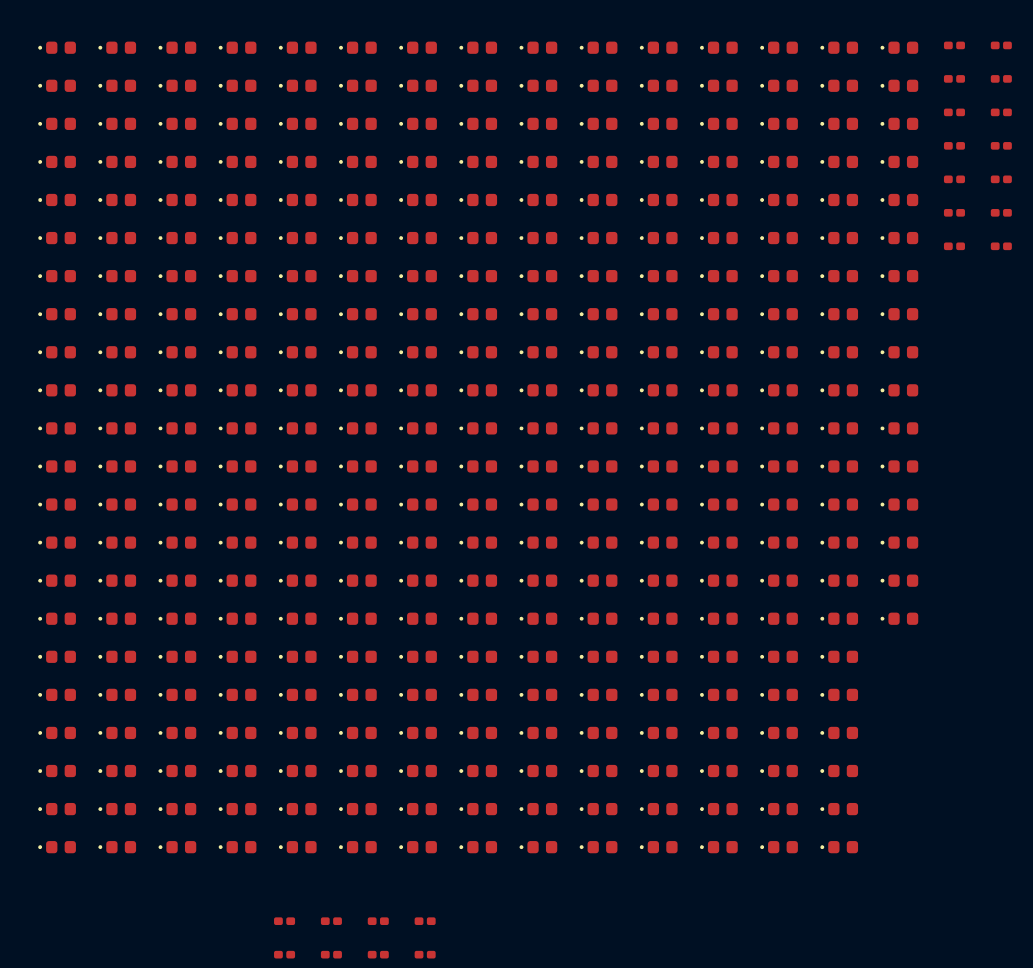
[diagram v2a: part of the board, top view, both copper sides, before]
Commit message: Renamed LED array due to kicad compatibility issues.
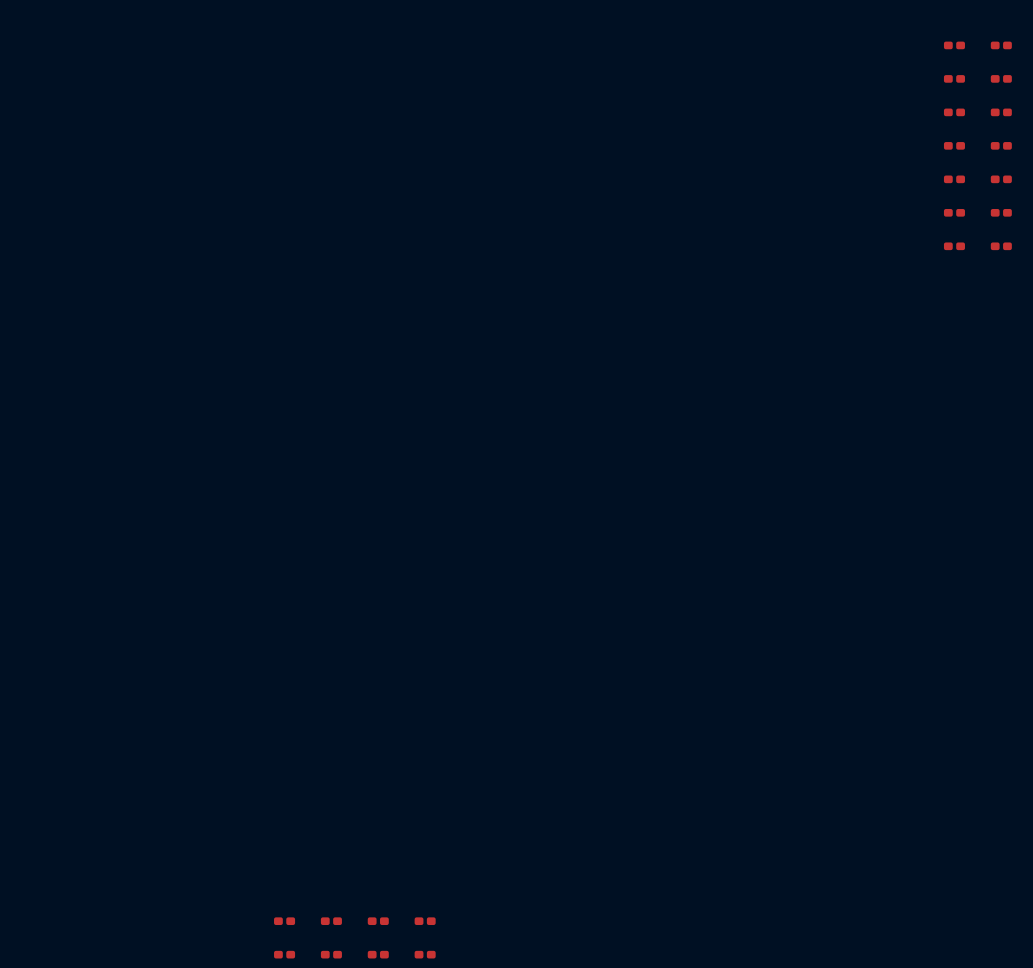
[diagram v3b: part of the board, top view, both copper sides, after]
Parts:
- removed D_0A1, D_0B1, D_0C1, D_0D1, D_0E1, D_0F1, D_0G1, D_0H1, D_1, D_10, D_100, D_11, D_12, D_13, D_14, D_15, D_16, D_17, D_18, D_19, D_1A1, D_1B1, D_1C1, D_1D1, D_1E1, D_1F1, D_1G1, D_1H1, D_2, D_20, D_21, D_22, D_23, D_24, D_25, D_26, D_27, D_28, D_29, D_2A1, D_2B1, D_2C1, D_2D1, D_2E1, D_2F1, D_2G1, D_2H1, D_3, D_30, D_31, D_32, D_33, D_34, D_35, D_36, D_37, D_38, D_39, D_3A1, D_3B1, D_3C1, D_3D1, D_3E1, D_3F1, D_3G1, D_3H1, D_4, D_40, D_41, D_42, D_43, D_44, D_45, D_46, D_47, D_48, D_49, D_4A1, D_4B1, D_4C1, D_4D1, D_4E1, D_4F1, D_4G1, D_4H1, D_5, D_50, D_51, D_52, D_53, D_54, D_55, D_56, D_57, D_58, D_59, D_5A1, D_5B1, D_5C1, D_5D1, D_5E1, D_5F1, D_5G1, D_5H1, D_6, D_60, D_61, D_62, D_63, D_64, D_65, D_66, D_67, D_68, D_69, D_6A1, D_6B1, D_6C1, D_6D1, D_6E1, D_6F1, D_6G1, D_6H1, D_7, D_70, D_71, D_72, D_73, D_74, D_75, D_76, D_77, D_78, D_79, D_7A1, D_7B1, D_7C1, D_7D1, D_7E1, D_7F1, D_7G1, D_7H1, D_8, D_80, D_81, D_82, D_83, D_84, D_85, D_86, D_87, D_88, D_89, D_8A1, D_8B1, D_8C1, D_8D1, D_8E1, D_8F1, D_8G1, D_8H1, D_9, D_90, D_91, D_92, D_93, D_94, D_95, D_96, D_97, D_98, D_99, D_9A1, D_9B1, D_9C1, D_9D1, D_9E1, D_9F1, D_9G1, D_9H1, D_A1, D_A10, D_A2, D_A3, D_A4, D_A5, D_A6, D_A7, D_A8, D_A9, D_AA1, D_AB1, D_AC1, D_AD1, D_AE1, D_AF1, D_AG1, D_AH1, D_B1, D_B10, D_B2, D_B3, D_B4, D_B5, D_B6, D_B7, D_B8, D_B9, D_BA1, D_BB1, D_BC1, D_BD1, D_BE1, D_BF1, D_BG1, D_BH1, D_C1, D_C10, D_C2, D_C3, D_C4, D_C5, D_C6, D_C7, D_C8, D_C9, D_CA1, D_CB1, D_CC1, D_CD1, D_CE1, D_CF1, D_CG1, D_CH1, D_D1, D_D10, D_D2, D_D3, D_D4, D_D5, D_D6, D_D7, D_D8, D_D9, D_DA1, D_DB1, D_DC1, D_DD1, D_DE1, D_DF1, D_DG1, D_DH1, D_E1, D_E10, D_E2, D_E3, D_E4, D_E5, D_E6, D_E7, D_E8, D_E9, D_EA1, D_EB1, D_EC1, D_ED1, D_EE1, D_EF1, D_EG1, D_EH1, D_F1, D_F10, D_F2, D_F3, D_F4, D_F5, D_F6, D_F7, D_F8, D_F9, D_FA1, D_FB1, D_FC1, D_FD1, D_FE1, D_FF1, D_FG1, D_FH1, D_G1, D_G10, D_G2, D_G3, D_G4, D_G5, D_G6, D_G7, D_G8, D_G9, D_GA1, D_GB1, D_GC1, D_GD1, D_GE1, D_GF1, D_GG1, D_GH1, D_H1, D_H10, D_H2, D_H3, D_H4, D_H5, D_H6, D_H7, D_H8, D_H9, D_HA1, D_HB1, D_HC1, D_HD1, D_HE1, D_HF1, D_HG1, D_HH1: LED, panel_custom:LED_0402_1005Metric
